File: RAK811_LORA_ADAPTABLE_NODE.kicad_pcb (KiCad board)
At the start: 2 copper layers, 75 x 49 mm, 23 parts, among them J1 Screw_Terminal_01x03, J10 Conn_01x09_Male, J11 Conn_01x09_Male, J12 Conn_01x09_Male, J2 Screw_Terminal_01x03, J3 Conn_01x03_Male, J4 Conn_01x03_Male, J5 Conn_01x11_Male, J6 Conn_01x01_Male, J7 Conn_Coaxial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

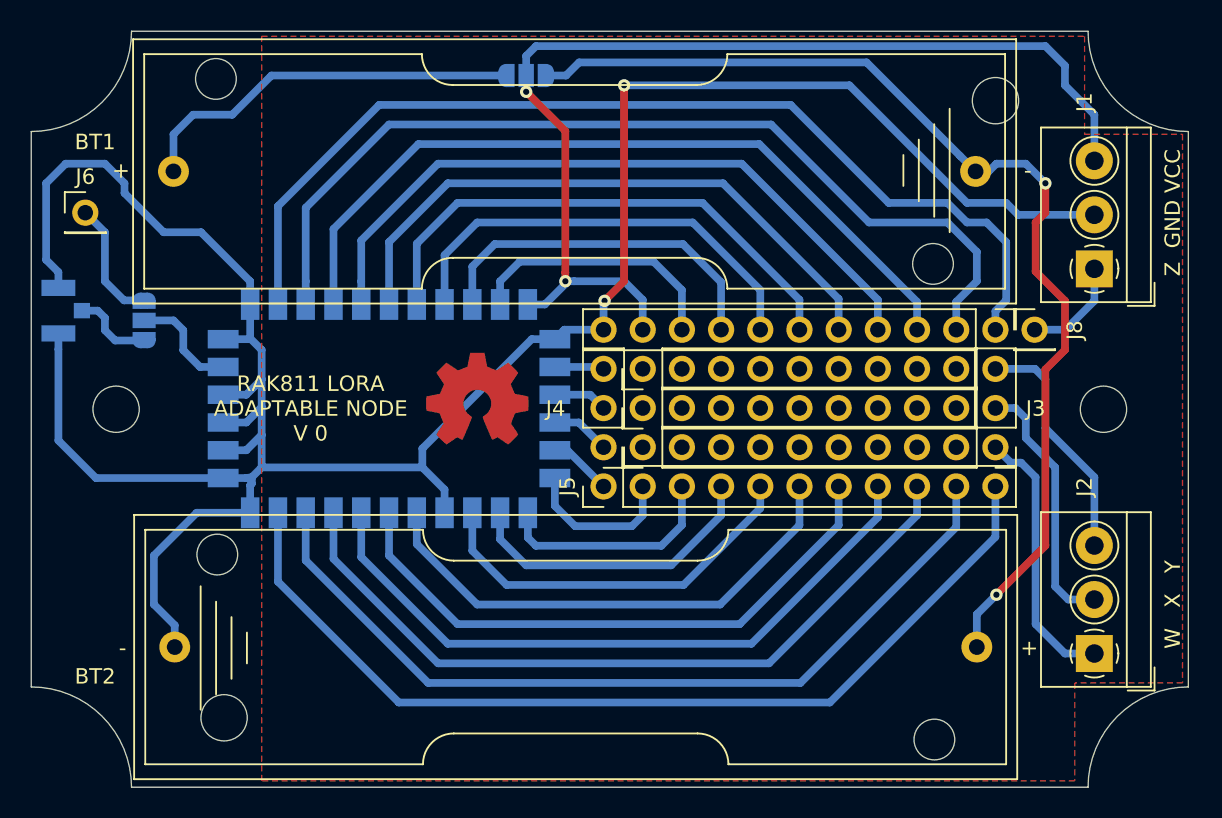
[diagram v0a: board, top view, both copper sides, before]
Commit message: shifted battery connector
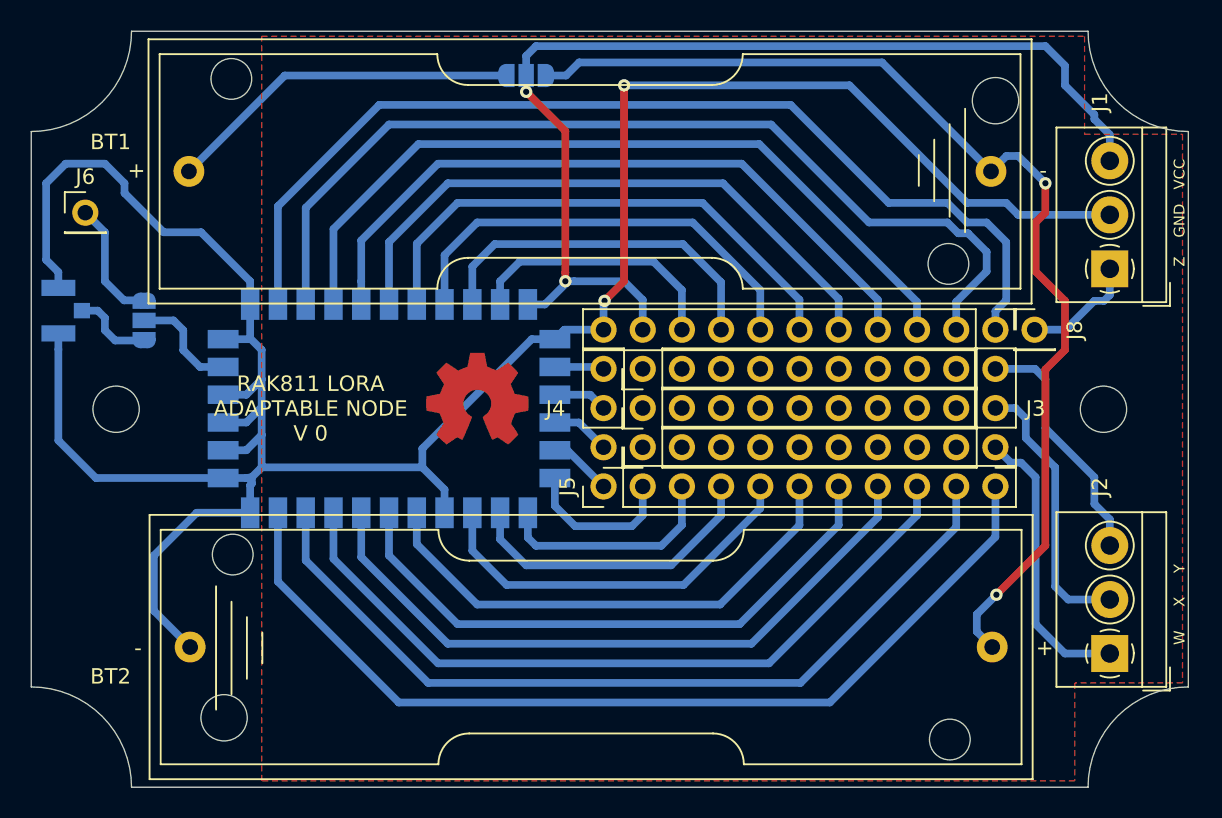
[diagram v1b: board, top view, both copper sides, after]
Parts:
- moved BT1 1.00 mm to (110.2, 109.1)
- moved BT2 1.00 mm to (162.3, 139.9)
- moved J1 1.00 mm to (169.9, 115.4)
- moved J2 1.00 mm to (169.9, 140.3)
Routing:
- net Net-(BT1-Pad1): track 25.5 -> 23.1 mm
- net Net-(BT2-Pad2): track 166.2 -> 167.6 mm
- net Net-(J2-Pad2): track 17.5 -> 18.5 mm
- net Net-(J8-Pad2): track 61.0 -> 61.9 mm
- net Net-(BT1-Pad2): track 69.8 -> 70.7 mm
- net Net-(J1-Pad1): track 6.72 -> 7.50 mm
